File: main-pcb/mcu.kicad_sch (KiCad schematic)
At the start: 74 parts, among them J11 CONN_01X03, J12 PMOD_HOST, J13 PMOD_HOST, J4 CORTEX_DEBUG_ETM, J5 CONN_01X03, U1 XC7S100-1FGGA484C, U12 AT24MAC402, U13 ECS-1612MV-250-CN, U14 STM32H735-UFBGA176-25, U15 S27KL0642GABHB020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

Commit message: Continued routing MCU
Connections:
- net FMC_A16: now also U1.J20 (IO_L17N_T2_15); no longer U1.K22 (IO_L22N_T3_15)
- net FMC_A22: now also U1.K19 (IO_L16N_T2_15); no longer U1.J19 (IO_L17P_T2_15)
- net FMC_A25: now also U1.K18 (IO_L16P_T2_15); no longer U1.J16 (IO_L5N_T0_AD9N_15)
- net FMC_AD1: now also U1.K22 (IO_L22N_T3_15); no longer U1.J15 (IO_L6N_T0_VREF_15)
- net FMC_AD12: now also U1.J17 (IO_L3P_T0_DQS_AD1P_15); no longer U1.K18 (IO_L16P_T2_15)
- net FMC_AD6: now also U1.G16 (IO_L4N_T0_15); no longer U1.K19 (IO_L16N_T2_15)
- net FMC_AD7: now also U1.J15 (IO_L6N_T0_VREF_15); no longer U1.H18 (IO_L3N_T0_DQS_AD1N_15)
- net FMC_AD8: now also U1.J16 (IO_L5N_T0_AD9N_15); no longer U1.G16 (IO_L4N_T0_15)
- net FMC_AD9: now also U1.H18 (IO_L3N_T0_DQS_AD1N_15); no longer U1.J20 (IO_L17N_T2_15)
- net FMC_NBL1: now also U1.J19 (IO_L17P_T2_15); no longer U1.J17 (IO_L3P_T0_DQS_AD1P_15)
- net MCU_LED_0: now also U14.N13 (PH8); no longer U14.M1 (PC2)
- net MCU_LED_1: now also U14.P13 (PE13); no longer U14.P11 (PF12)
- net MCU_LED_2: now also U14.P12 (PE12); no longer U14.N15 (PH12)
- net MCU_LED_3: now also U14.N12 (PB10); no longer U14.P15 (PH6)
- net MCU_PMOD_DQ0: now also U14.M15 (PB12); no longer U14.P10 (PB11)
- net MCU_PMOD_DQ1: now also U14.N15 (PH12); no longer U14.R10 (PF14)
- net MCU_PMOD_DQ2: now also U14.R6 (PC4); no longer U14.M15 (PB12)
- net MCU_PMOD_DQ3: now also U14.P5 (PA4); no longer U14.M7 (PC5)
- net MCU_PMOD_DQ4: now also U14.L15 (PB13); no longer U14.P12 (PE12)
- net MCU_PMOD_DQ5: now also U14.N14 (PH10); no longer U14.P13 (PE13)
- net MCU_PMOD_DQ6: now also U14.P15 (PH6); no longer U14.R8 (PB0)
- net MCU_PMOD_DQ7: now also U14.R4 (PH3); no longer U14.R6 (PC4)
- net PRSNT_1V2: now also U14.M2 (PC3); no longer U14.P5 (PA4)
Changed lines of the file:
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@@
 	)
 	(no_connect
+		(at 143.51 31.75)
+	)
+	(no_connect
 		(at 195.58 91.44)
 	)
@@
 	)
 	(no_connect
-		(at 100.33 57.15)
-	)
-	(no_connect
 		(at 143.51 121.92)
 	)
@@
 	)
 	(no_connect
+		(at 143.51 44.45)
+	)
+	(no_connect
 		(at 143.51 52.07)
 	)
@@
 	)
 	(no_connect
-		(at 143.51 111.76)
+		(at 195.58 104.14)
 	)
 	(no_connect
-		(at 195.58 104.14)
+		(at 100.33 116.84)
 	)
 	(no_connect
@@
 	)
 	(no_connect
-		(at 100.33 64.77)
-	)
-	(no_connect
 		(at 100.33 46.99)
 	)
@@
 	)
 	(no_connect
-		(at 143.51 36.83)
-	)
-	(no_connect
 		(at 163.83 247.65)
 	)
@@
 	)
 	(no_connect
+		(at 100.33 59.69)
+	)
+	(no_connect
 		(at 143.51 124.46)
 	)
@@
 	)
 	(no_connect
-		(at 143.51 93.98)
-	)
-	(no_connect
 		(at 143.51 109.22)
 	)
@@
 	)
 	(no_connect
+		(at 100.33 31.75)
+	)
+	(no_connect
+		(at 100.33 121.92)
+	)
+	(no_connect
 		(at 143.51 114.3)
 	)
@@
 	)
 	(no_connect
-		(at 143.51 106.68)
-	)
-	(no_connect
 		(at 143.51 54.61)
 	)
@@
 	)
 	(label "MCU_PMOD_DQ2"
-		(at 100.33 62.23 180)
+		(at 143.51 41.91 180)
 		(fields_autoplaced yes)
 		(effects
@@
 	)
 	(label "MCU_PMOD_DQ4"
-		(at 49.53 116.84 180)
+		(at 100.33 64.77 180)
 		(fields_autoplaced yes)
 		(effects
@@
 	)
 	(label "MCU_PMOD_DQ1"
-		(at 100.33 121.92 180)
+		(at 143.51 116.84 180)
 		(fields_autoplaced yes)
 		(effects
@@
 	)
 	(label "MCU_LED_3"
-		(at 143.51 101.6 180)
+		(at 100.33 57.15 180)
 		(fields_autoplaced yes)
 		(effects
@@
 	)
 	(label "MCU_PMOD_DQ5"
-		(at 49.53 119.38 180)
+		(at 143.51 111.76 180)
 		(fields_autoplaced yes)
 		(effects
@@
 	)
 	(label "FMC_A16"
-		(at 353.06 165.1 180)
+		(at 353.06 139.7 180)
 		(fields_autoplaced yes)
 		(effects
@@
 	)
 	(label "MCU_PMOD_DQ6"
-		(at 100.33 31.75 180)
+		(at 143.51 101.6 180)
 		(fields_autoplaced yes)
 		(effects
@@
 	)
 	(label "FMC_AD1"
-		(at 353.06 83.82 180)
+		(at 353.06 165.1 180)
 		(fields_autoplaced yes)
 		(effects
@@
 	)
 	(label "MCU_LED_2"
-		(at 143.51 116.84 180)
+		(at 49.53 116.84 180)
 		(fields_autoplaced yes)
 		(effects
@@
 	)
 	(label "MCU_PMOD_DQ0"
-		(at 100.33 59.69 180)
+		(at 100.33 62.23 180)
 		(fields_autoplaced yes)
 		(effects
@@
 	)
 	(label "MCU_LED_0"
-		(at 143.51 31.75 180)
+		(at 143.51 106.68 180)
 		(fields_autoplaced yes)
 		(effects
@@
 	)
 	(label "MCU_PMOD_DQ3"
-		(at 143.51 44.45 180)
+		(at 49.53 41.91 180)
 		(fields_autoplaced yes)
 		(effects
@@
 	)
 	(label "FMC_A25"
-		(at 353.06 78.74 180)
+		(at 353.06 132.08 180)
 		(fields_autoplaced yes)
 		(effects
@@
 	)
 	(label "FMC_AD7"
-		(at 353.06 68.58 180)
+		(at 353.06 83.82 180)
 		(fields_autoplaced yes)
 		(effects
@@
 	)
 	(label "FMC_AD6"
-		(at 353.06 134.62 180)
+		(at 353.06 73.66 180)
 		(fields_autoplaced yes)
 		(effects
@@
 	)
 	(label "FMC_NBL1"
-		(at 353.06 66.04 180)
+		(at 353.06 137.16 180)
 		(fields_autoplaced yes)
 		(effects
@@
 	)
 	(label "FMC_AD12"
-		(at 353.06 132.08 180)
+		(at 353.06 66.04 180)
 		(fields_autoplaced yes)
 		(effects
@@
 	)
 	(label "FMC_AD9"
-		(at 353.06 139.7 180)
+		(at 353.06 68.58 180)
 		(fields_autoplaced yes)
 		(effects
@@
 	)
 	(label "FMC_A22"
-		(at 353.06 137.16 180)
+		(at 353.06 134.62 180)
 		(fields_autoplaced yes)
 		(effects
@@
 	)
 	(label "FMC_AD8"
-		(at 353.06 73.66 180)
+		(at 353.06 78.74 180)
 		(fields_autoplaced yes)
 		(effects
@@
 	)
 	(label "MCU_PMOD_DQ7"
-		(at 143.51 41.91 180)
+		(at 143.51 93.98 180)
 		(fields_autoplaced yes)
 		(effects
@@
 	)
 	(label "MCU_LED_1"
-		(at 100.33 116.84 180)
+		(at 49.53 119.38 180)
 		(fields_autoplaced yes)
 		(effects
@@
 	(hierarchical_label "PRSNT_1V2"
 		(shape input)
-		(at 49.53 41.91 180)
+		(at 143.51 36.83 180)
 		(fields_autoplaced yes)
 		(effects

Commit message: 500 unrouted, still lots more to go
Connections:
- net FPGA_DONE: now also U14.C14 (PA10); no longer U14.P1 (PA0)
- net FPGA_LED_0: now also U1.L15 (IO_L13N_T2_MRCC_15); no longer U1.M17 (IO_L14P_T2_SRCC_15)
- net FPGA_LED_1: now also U1.L16 (IO_L15P_T2_DQS_15); no longer U1.M18 (IO_L14N_T2_SRCC_15)
- net FPGA_LED_2: now also U1.M16 (IO_25_15); no longer U1.K17 (IO_L15N_T2_DQS_15)
- net FPGA_LED_3: now also U1.M17 (IO_L14P_T2_SRCC_15); no longer U1.L16 (IO_L15P_T2_DQS_15)
- net FPGA_PMOD_DQ0: now also U1.K17 (IO_L15N_T2_DQS_15); no longer U1.L22 (IO_L22P_T3_15)
- net FPGA_PMOD_DQ1: now also U1.L22 (IO_L22P_T3_15); no longer U1.K16 (IO_L5P_T0_AD9P_15)
- net FPGA_PMOD_DQ2: now also U1.L20 (IO_L24P_T3_RS1_15); no longer U1.L18 (IO_L18P_T2_15)
- net FPGA_PMOD_DQ3: now also U1.M18 (IO_L14N_T2_SRCC_15); no longer U1.L19 (IO_L18N_T2_15)
- net FPGA_PMOD_DQ4: now also U1.K16 (IO_L5P_T0_AD9P_15); no longer U1.L20 (IO_L24P_T3_RS1_15)
- net FPGA_PMOD_DQ5: now also U1.L18 (IO_L18P_T2_15); no longer U1.L21 (IO_L24N_T3_RS0_15)
- net FPGA_PMOD_DQ6: now also U1.L21 (IO_L24N_T3_RS0_15); no longer U1.M16 (IO_25_15)
- net FPGA_PMOD_DQ7: now also U1.L19 (IO_L18N_T2_15); no longer U1.L15 (IO_L13N_T2_MRCC_15)
- net PRSNT_1V2: now also U14.B10 (PD2); no longer U14.M2 (PC3)
- net PRSNT_1V8: now also U14.B11 (PC12); no longer U14.N5 (PA3)
- net PRSNT_2V5: now also U14.C13 (PH13); no longer U14.R2 (PA2)
- net PRSNT_3V3: now also U14.C12 (PC10); no longer U14.P2 (PA1)
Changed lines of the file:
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@@
 	)
 	(no_connect
-		(at 143.51 119.38)
-	)
-	(no_connect
 		(at 195.58 93.98)
 	)
@@
 	)
 	(no_connect
-		(at 143.51 57.15)
-	)
-	(no_connect
 		(at 100.33 34.29)
 	)
@@
 	)
 	(no_connect
-		(at 143.51 29.21)
+		(at 49.53 36.83)
 	)
 	(no_connect
-		(at 49.53 57.15)
+		(at 143.51 29.21)
 	)
 	(no_connect
-		(at 143.51 62.23)
+		(at 49.53 26.67)
 	)
 	(no_connect
@@
 	)
 	(no_connect
+		(at 143.51 36.83)
+	)
+	(no_connect
 		(at 49.53 34.29)
 	)
@@
 	)
 	(no_connect
+		(at 49.53 39.37)
+	)
+	(no_connect
 		(at 241.3 236.22)
 	)
@@
 	)
 	(no_connect
-		(at 195.58 36.83)
+		(at 100.33 31.75)
 	)
 	(no_connect
-		(at 100.33 31.75)
+		(at 49.53 31.75)
 	)
 	(no_connect
@@
 	)
 	(label "FPGA_PMOD_DQ4"
-		(at 353.06 172.72 180)
+		(at 353.06 76.2 180)
 		(fields_autoplaced yes)
 		(effects
@@
 	)
 	(label "FPGA_PMOD_DQ1"
-		(at 353.06 76.2 180)
+		(at 353.06 162.56 180)
 		(fields_autoplaced yes)
 		(effects
@@
 	)
 	(label "FPGA_LED_0"
-		(at 353.06 121.92 180)
+		(at 353.06 119.38 180)
 		(fields_autoplaced yes)
 		(effects
@@
 	)
 	(label "FPGA_PMOD_DQ2"
-		(at 353.06 142.24 180)
+		(at 353.06 172.72 180)
 		(fields_autoplaced yes)
 		(effects
@@
 	)
 	(label "FPGA_LED_3"
-		(at 353.06 127 180)
+		(at 353.06 121.92 180)
 		(fields_autoplaced yes)
 		(effects
@@
 	)
 	(label "FPGA_PMOD_DQ7"
-		(at 353.06 119.38 180)
+		(at 353.06 144.78 180)
 		(fields_autoplaced yes)
 		(effects
@@
 	)
 	(label "FPGA_LED_2"
-		(at 353.06 129.54 180)
+		(at 353.06 177.8 180)
 		(fields_autoplaced yes)
 		(effects
@@
 	)
 	(label "FPGA_PMOD_DQ0"
-		(at 353.06 162.56 180)
+		(at 353.06 129.54 180)
 		(fields_autoplaced yes)
 		(effects
@@
 	)
 	(label "FPGA_PMOD_DQ5"
-		(at 353.06 175.26 180)
+		(at 353.06 142.24 180)
 		(fields_autoplaced yes)
 		(effects
@@
 	)
 	(label "FPGA_PMOD_DQ6"
-		(at 353.06 177.8 180)
+		(at 353.06 175.26 180)
 		(fields_autoplaced yes)
 		(effects
@@
 	)
 	(label "FPGA_LED_1"
-		(at 353.06 124.46 180)
+		(at 353.06 127 180)
 		(fields_autoplaced yes)
 		(effects
@@
 	)
 	(label "FPGA_PMOD_DQ3"
-		(at 353.06 144.78 180)
+		(at 353.06 124.46 180)
 		(fields_autoplaced yes)
 		(effects
@@
 	(hierarchical_label "PRSNT_2V5"
 		(shape input)
-		(at 49.53 36.83 180)
+		(at 143.51 119.38 180)
 		(fields_autoplaced yes)
 		(effects
@@
 	(hierarchical_label "PRSNT_1V8"
 		(shape input)
-		(at 49.53 39.37 180)
+		(at 143.51 62.23 180)
 		(fields_autoplaced yes)
 		(effects
@@
 	(hierarchical_label "PRSNT_1V2"
 		(shape input)
-		(at 143.51 36.83 180)
+		(at 195.58 36.83 180)
 		(fields_autoplaced yes)
 		(effects
@@
 	(hierarchical_label "FPGA_DONE"
 		(shape input)
-		(at 49.53 26.67 180)
+		(at 49.53 57.15 180)
 		(fields_autoplaced yes)
 		(effects
@@
 	(hierarchical_label "PRSNT_3V3"
 		(shape input)
-		(at 49.53 31.75 180)
+		(at 143.51 57.15 180)
 		(fields_autoplaced yes)
 		(effects

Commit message: Almost fully routed MCU
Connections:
- net PRSNT_1V2: now also U14.C13 (PH13); no longer U14.B10 (PD2)
- net PRSNT_1V8: now also U14.C12 (PC10); no longer U14.B11 (PC12)
- net PRSNT_2V5: now also U14.B11 (PC12); no longer U14.C13 (PH13)
- net PRSNT_3V3: now also U14.B10 (PD2); no longer U14.C12 (PC10)
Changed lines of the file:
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@@
 	(hierarchical_label "PRSNT_2V5"
 		(shape input)
-		(at 143.51 119.38 180)
+		(at 143.51 62.23 180)
 		(fields_autoplaced yes)
 		(effects
@@
 	(hierarchical_label "PRSNT_1V8"
 		(shape input)
-		(at 143.51 62.23 180)
+		(at 143.51 57.15 180)
 		(fields_autoplaced yes)
 		(effects
@@
 	(hierarchical_label "PRSNT_1V2"
 		(shape input)
-		(at 195.58 36.83 180)
+		(at 143.51 119.38 180)
 		(fields_autoplaced yes)
 		(effects
@@
 	(hierarchical_label "PRSNT_3V3"
 		(shape input)
-		(at 143.51 57.15 180)
+		(at 195.58 36.83 180)
 		(fields_autoplaced yes)
 		(effects

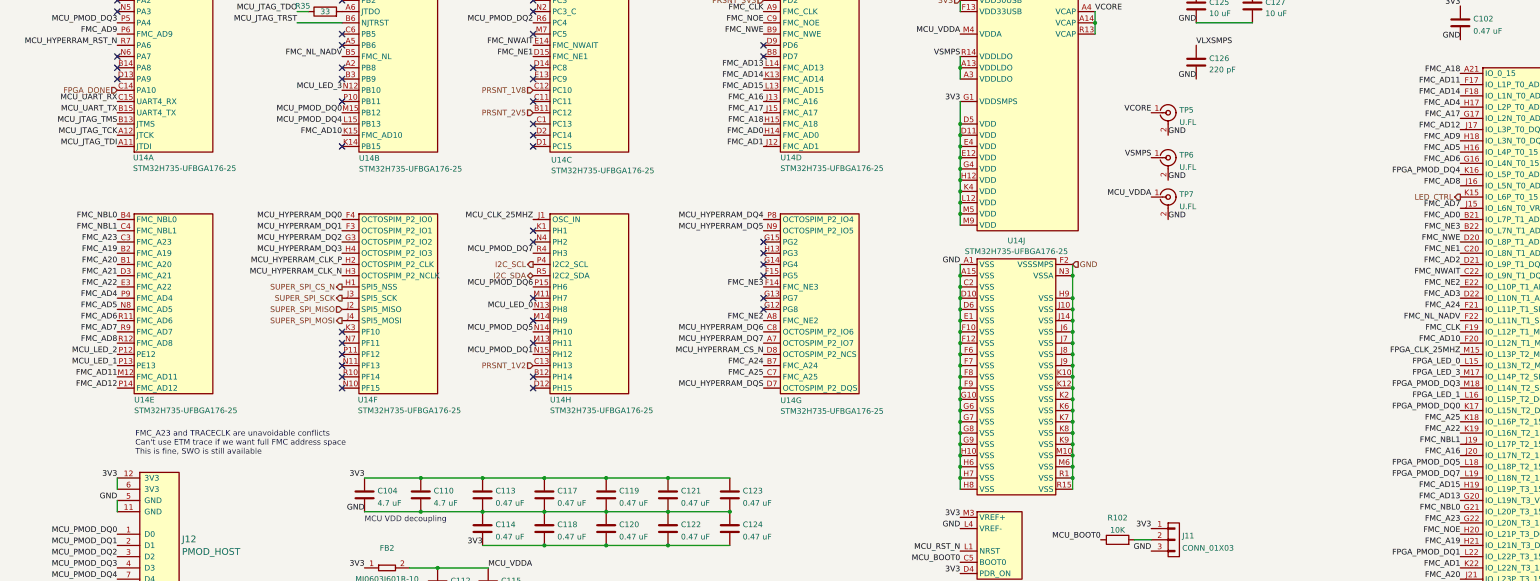
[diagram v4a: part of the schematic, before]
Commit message: Routing cleanup around MCU, fixed some DRC errors
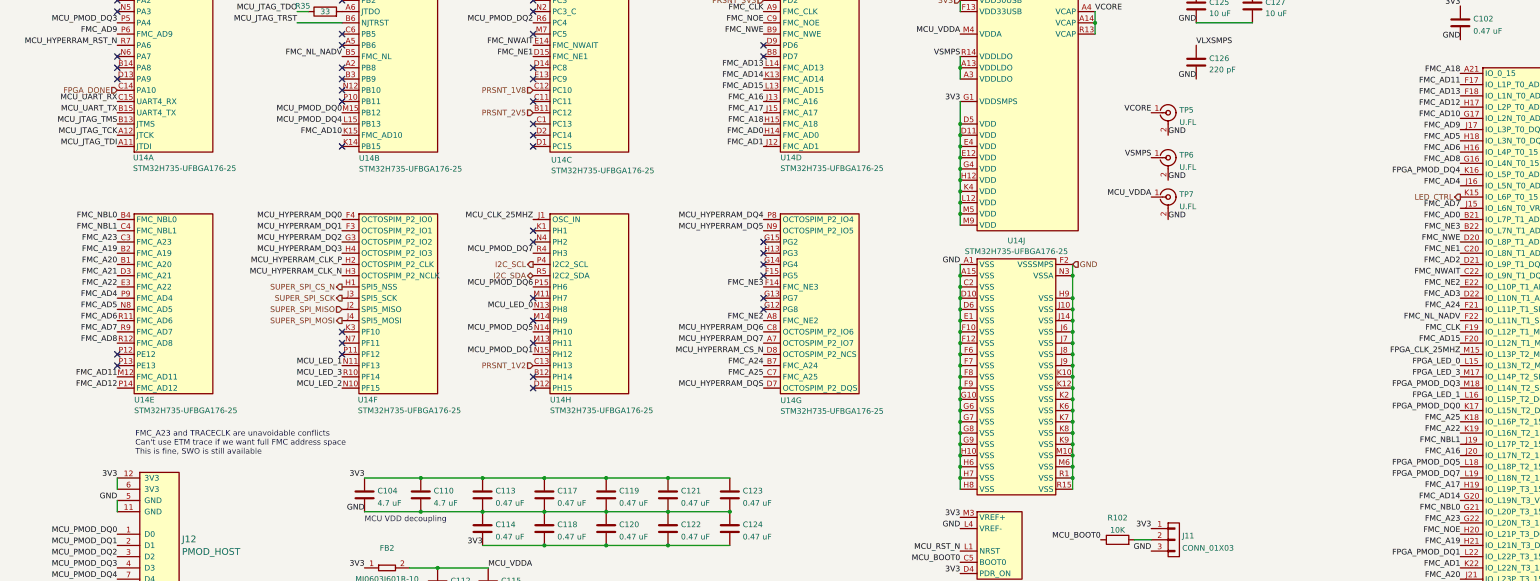
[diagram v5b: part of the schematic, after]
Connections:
- net FMC_A17: now also U1.H19 (IO_L19P_T3_15); no longer U1.G17 (IO_L2N_T0_AD8N_15)
- net FMC_AD10: now also U1.G17 (IO_L2N_T0_AD8N_15); no longer U1.F20 (IO_L12N_T1_MRCC_15)
- net FMC_AD12: now also U1.H17 (IO_L2P_T0_AD8P_15); no longer U1.J17 (IO_L3P_T0_DQS_AD1P_15)
- net FMC_AD13: now also U1.F18 (IO_L1N_T0_AD0N_15); no longer U1.G20 (IO_L19N_T3_VREF_15)
- net FMC_AD14: now also U1.G20 (IO_L19N_T3_VREF_15); no longer U1.F18 (IO_L1N_T0_AD0N_15)
- net FMC_AD15: now also U1.F20 (IO_L12N_T1_MRCC_15); no longer U1.H19 (IO_L19P_T3_15)
- net FMC_AD4: now also U1.J16 (IO_L5N_T0_AD9N_15); no longer U1.H17 (IO_L2P_T0_AD8P_15)
- net FMC_AD5: now also U1.H18 (IO_L3N_T0_DQS_AD1N_15); no longer U1.H16 (IO_L4P_T0_15)
- net FMC_AD6: now also U1.H16 (IO_L4P_T0_15); no longer U1.G16 (IO_L4N_T0_15)
- net FMC_AD8: now also U1.G16 (IO_L4N_T0_15); no longer U1.J16 (IO_L5N_T0_AD9N_15)
- net FMC_AD9: now also U1.J17 (IO_L3P_T0_DQS_AD1P_15); no longer U1.H18 (IO_L3N_T0_DQS_AD1N_15)
- net MCU_LED_1: now also U14.N11 (PF13); no longer U14.P13 (PE13)
- net MCU_LED_2: now also U14.N10 (PF15); no longer U14.P12 (PE12)
- net MCU_LED_3: now also U14.R10 (PF14); no longer U14.N12 (PB10)
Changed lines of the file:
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@@
 	(title_block
 		(title "DUMPTRUCK flash dumper")
-		(date "2024-10-23")
+		(date "2024-10-24")
 		(rev "0.1")
 		(company "Antikernel Labs")
@@
 	)
 	(no_connect
+		(at 100.33 57.15)
+	)
+	(no_connect
 		(at 195.58 93.98)
 	)
@@
 	)
 	(no_connect
-		(at 100.33 124.46)
+		(at 49.53 116.84)
 	)
 	(no_connect
@@
 	)
 	(no_connect
+		(at 49.53 119.38)
+	)
+	(no_connect
 		(at 100.33 52.07)
 	)
@@
 	)
 	(no_connect
-		(at 100.33 119.38)
-	)
-	(no_connect
 		(at 100.33 59.69)
 	)
@@
 	)
 	(no_connect
-		(at 100.33 121.92)
-	)
-	(no_connect
 		(at 143.51 114.3)
 	)
@@
 	)
 	(label "FMC_AD10"
-		(at 353.06 114.3 180)
+		(at 353.06 63.5 180)
 		(fields_autoplaced yes)
 		(effects
@@
 	)
 	(label "MCU_LED_3"
-		(at 100.33 57.15 180)
+		(at 100.33 121.92 180)
 		(fields_autoplaced yes)
 		(effects
@@
 	)
 	(label "FMC_A17"
-		(at 353.06 63.5 180)
+		(at 353.06 147.32 180)
 		(fields_autoplaced yes)
 		(effects
@@
 	)
 	(label "FMC_AD13"
-		(at 353.06 149.86 180)
+		(at 353.06 58.42 180)
 		(fields_autoplaced yes)
 		(effects
@@
 	)
 	(label "MCU_LED_2"
-		(at 49.53 116.84 180)
+		(at 100.33 124.46 180)
 		(fields_autoplaced yes)
 		(effects
@@
 	)
 	(label "FMC_AD15"
-		(at 353.06 147.32 180)
+		(at 353.06 114.3 180)
 		(fields_autoplaced yes)
 		(effects
@@
 	)
 	(label "FMC_AD6"
-		(at 353.06 73.66 180)
+		(at 353.06 71.12 180)
 		(fields_autoplaced yes)
 		(effects
@@
 	)
 	(label "FMC_AD12"
-		(at 353.06 66.04 180)
+		(at 353.06 60.96 180)
 		(fields_autoplaced yes)
 		(effects
@@
 	)
 	(label "FMC_AD9"
-		(at 353.06 68.58 180)
+		(at 353.06 66.04 180)
 		(fields_autoplaced yes)
 		(effects
@@
 	)
 	(label "FMC_AD14"
-		(at 353.06 58.42 180)
+		(at 353.06 149.86 180)
 		(fields_autoplaced yes)
 		(effects
@@
 	)
 	(label "FMC_AD8"
-		(at 353.06 78.74 180)
+		(at 353.06 73.66 180)
 		(fields_autoplaced yes)
 		(effects
@@
 	)
 	(label "MCU_LED_1"
-		(at 49.53 119.38 180)
+		(at 100.33 119.38 180)
 		(fields_autoplaced yes)
 		(effects
@@
 	)
 	(label "FMC_AD5"
-		(at 353.06 71.12 180)
+		(at 353.06 68.58 180)
 		(fields_autoplaced yes)
 		(effects
@@
 	)
 	(label "FMC_AD4"
-		(at 353.06 60.96 180)
+		(at 353.06 78.74 180)
 		(fields_autoplaced yes)
 		(effects
